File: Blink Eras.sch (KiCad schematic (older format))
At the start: 12 parts, among them IC1 ATTINY85-M, P1 CONN_02X03, U1 ICM7555

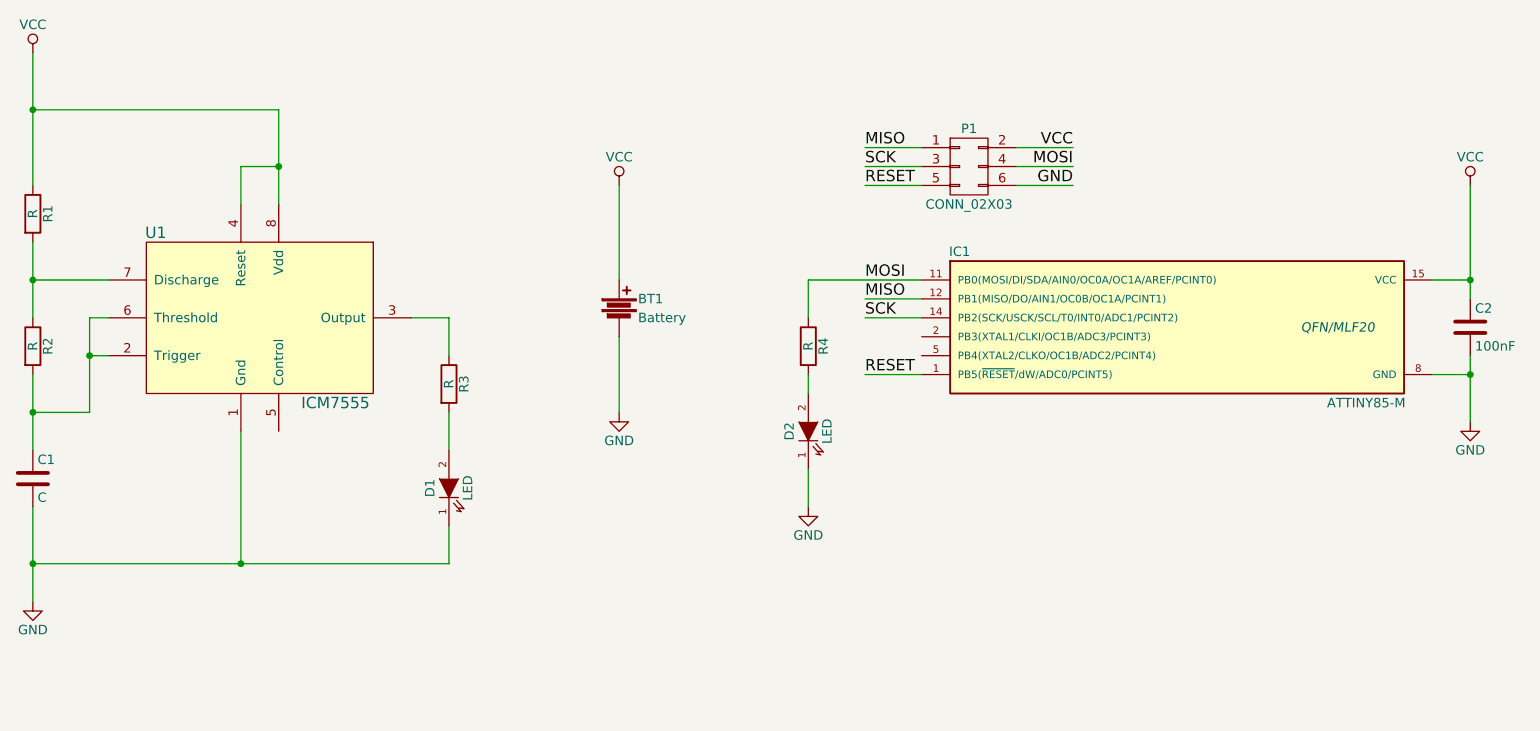
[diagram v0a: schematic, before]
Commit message: Schematic cleanup.  Passes ERC.
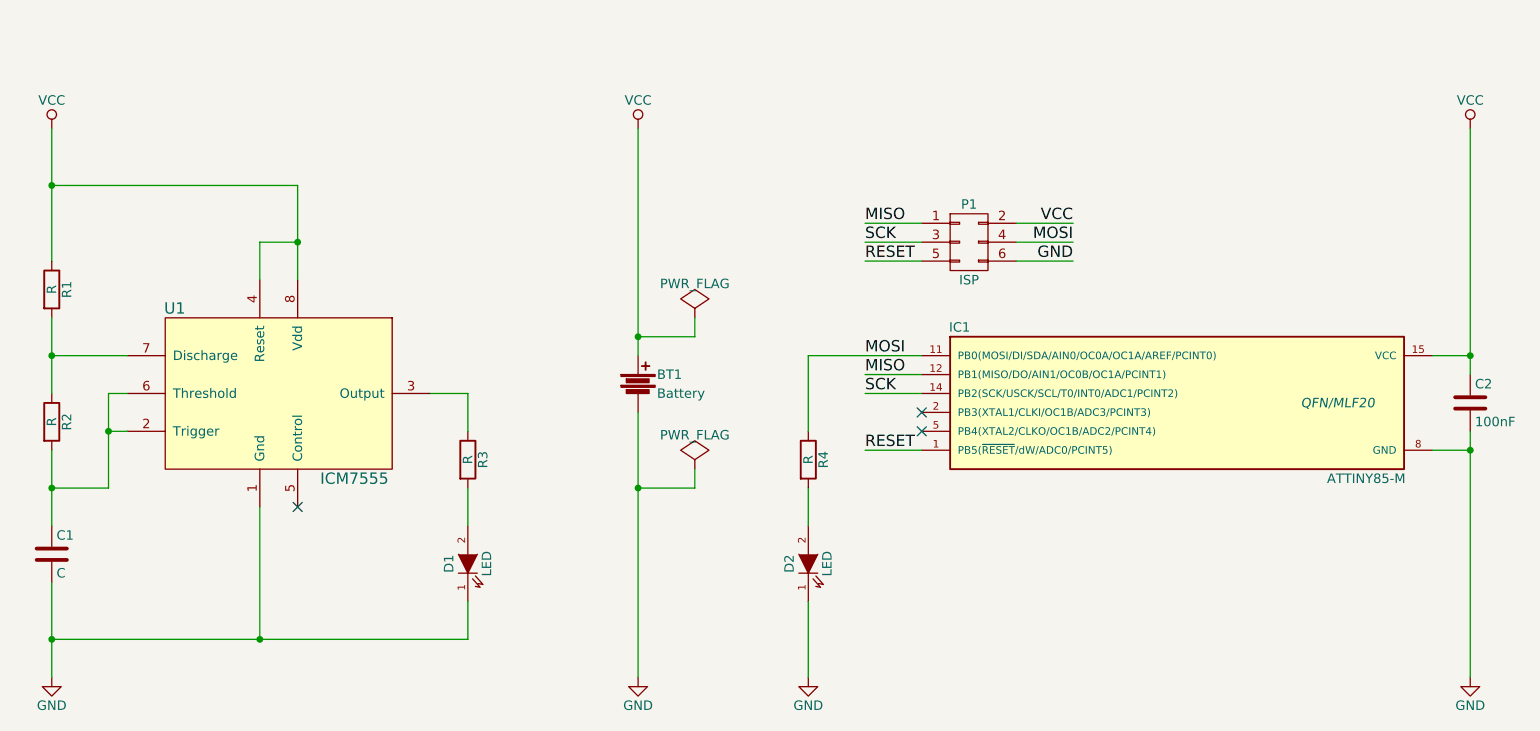
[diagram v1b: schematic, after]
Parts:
- P1: value CONN_02X03 -> ISP
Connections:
- no-connect marks 0 -> 3
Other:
- moved on the sheet: BT1, C1, C2, D1, D2, IC1, P1, R1, R2, R3, R4, U1
